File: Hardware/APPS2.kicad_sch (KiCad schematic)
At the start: 18 parts, among them U18 MCP6N11-005, U21 MCP6001

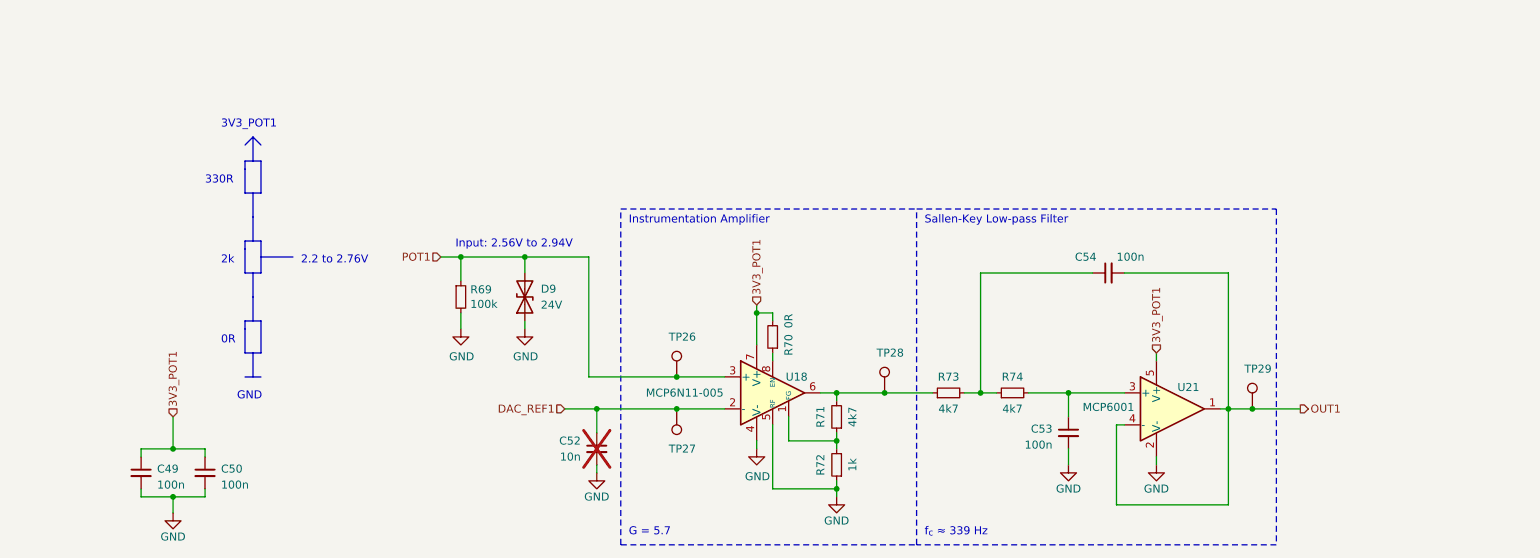
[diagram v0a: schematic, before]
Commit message: Created new hardware version 2.0
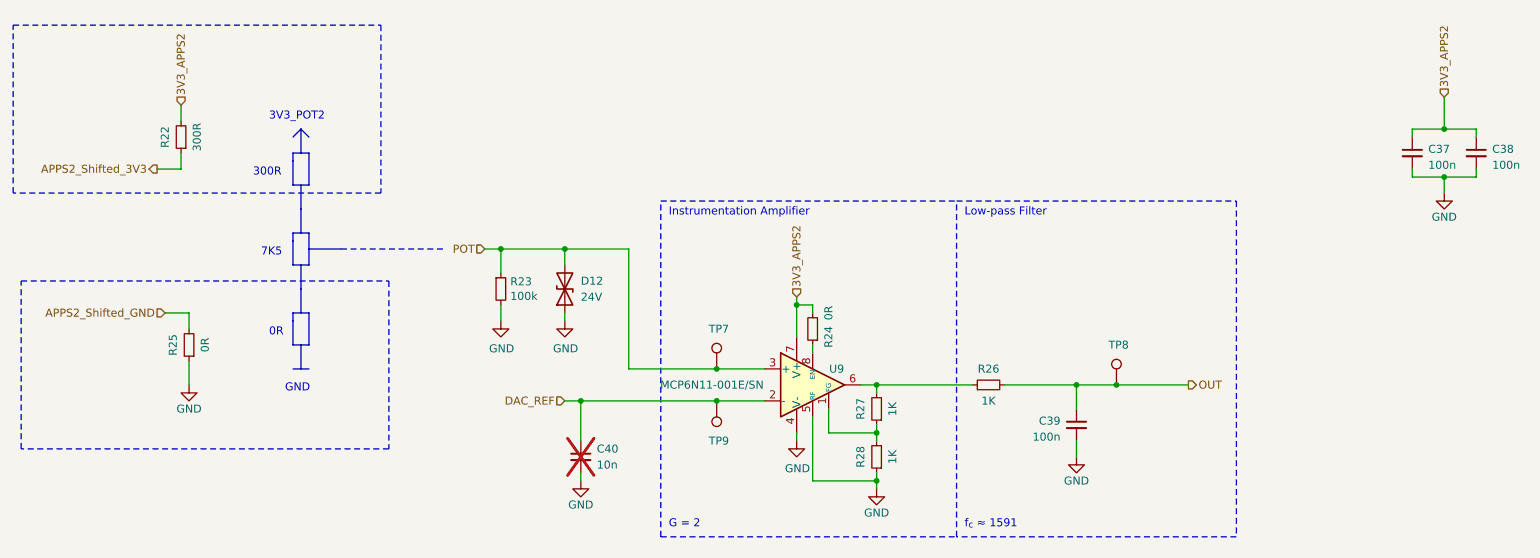
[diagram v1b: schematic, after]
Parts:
- removed C49, C50, C53, C54: 100n, Capacitor_SMD:C_0603_1608Metric_Pad1.08x0.95mm_HandSolder, symbol Device:C_Small
- removed C52: 10n, Capacitor_SMD:C_0603_1608Metric_Pad1.08x0.95mm_HandSolder, symbol Device:C_Small
- removed D9: 24V, Diode_SMD:D_0603_1608Metric_Pad1.05x0.95mm_HandSolder, symbol Device:D_TVS
- removed R69: 100k, Resistor_SMD:R_0603_1608Metric_Pad0.98x0.95mm_HandSolder, symbol Device:R_Small
- removed R70: 0R, Resistor_SMD:R_0603_1608Metric_Pad0.98x0.95mm_HandSolder, symbol Device:R_Small
- removed R71, R73, R74: 4k7, Resistor_SMD:R_0603_1608Metric_Pad0.98x0.95mm_HandSolder, symbol Device:R_Small
- removed R72: 1k, Resistor_SMD:R_0603_1608Metric_Pad0.98x0.95mm_HandSolder, symbol Device:R_Small
- removed TP26: APPS_P, TestPoint:TestPoint_Pad_D1.0mm, symbol Connector:TestPoint
- removed TP27: APPS_N, TestPoint:TestPoint_Pad_D1.0mm, symbol Connector:TestPoint
- removed TP28: APPS_MID, TestPoint:TestPoint_Pad_D1.0mm, symbol Connector:TestPoint
- removed TP29: APPS_OUT, TestPoint:TestPoint_Pad_D1.0mm, symbol Connector:TestPoint
- removed U18: MCP6N11-005, Package_DFN_QFN:TDFN-8-1EP_3x2mm_P0.5mm_EP1.3x1.4mm, symbol MCP6N11:MCP6N11
- removed U21: MCP6001, Package_TO_SOT_SMD:SOT-23-5, symbol Amplifier_Operational:MCP6001-OT
- added C37, C38, C39: 100n, Capacitor_SMD:C_0603_1608Metric_Pad1.08x0.95mm_HandSolder, symbol Device:C_Small
- added C40: 10n, Capacitor_SMD:C_0603_1608Metric_Pad1.08x0.95mm_HandSolder, symbol Device:C_Small
- added D12: 24V, Diode_SMD:D_0603_1608Metric_Pad1.05x0.95mm_HandSolder, symbol Device:D_TVS
- added R22: 300R, Resistor_SMD:R_0603_1608Metric_Pad0.98x0.95mm_HandSolder, symbol Device:R_Small
- added R23: 100k, Resistor_SMD:R_0603_1608Metric_Pad0.98x0.95mm_HandSolder, symbol Device:R_Small
- added R24, R25: 0R, Resistor_SMD:R_0603_1608Metric_Pad0.98x0.95mm_HandSolder, symbol Device:R_Small
- added R26, R27, R28: 1K, Resistor_SMD:R_0603_1608Metric_Pad0.98x0.95mm_HandSolder, symbol Device:R_Small
- added TP7: APPS_P, TestPoint:TestPoint_THTPad_D1.0mm_Drill0.5mm, symbol Connector:TestPoint
- added TP8: APPS_OUT, TestPoint:TestPoint_THTPad_D1.0mm_Drill0.5mm, symbol Connector:TestPoint
- added TP9: APPS_N, TestPoint:TestPoint_THTPad_D1.0mm_Drill0.5mm, symbol Connector:TestPoint
- added U9: MCP6N11-001E/SN, Package_SO:SOIC-8_3.9x4.9mm_P1.27mm, symbol MCP6N11:MCP6N11
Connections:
- net GND: now also C37.2, C38.2, C39.2, C40.2, D12.1 (A1), R23.2, R25.1, R28.1, U9.4 (V-), U9.5 (RF)
- new net: R26.1, R27.2, U9.6
- new net: R27.1, R28.2, U9.1 (FG)
- new net: R24.1, U9.8 (EN)
- new net 3V3_APPS2: C37.1, C38.1, R22.2, R24.2, U9.7 (V+)
- new net APPS2_Shifted_3V3: R22.1
- new net APPS2_Shifted_GND: R25.2
- new net DAC_REF: C40.1, TP9.1, U9.2 (-)
- new net OUT: C39.1, R26.2, TP8.1
- new net POT: D12.2 (A2), R23.1, TP7.1, U9.3 (+)
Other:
- note added: "300R"
- note added: "3V3_POT2"
- note added: "7K5"
- note added: "G = 2"
- note added: "Low-pass Filter"
- note added: "f_{c} ≈ 1591"
- note removed: "2.2 to 2.76V"
- note removed: "2k"
- note removed: "330R"
- note removed: "3V3_POT1"
- note removed: "G = 5.7"
- note removed: "Input: 2.56V to 2.94V"
- note removed: "Sallen-Key Low-pass Filter"
- note removed: "f_{c} ≈ 339 Hz"

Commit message: Changes in schematic, separated CAN buses, added XIAO Sense S3 DevBoard
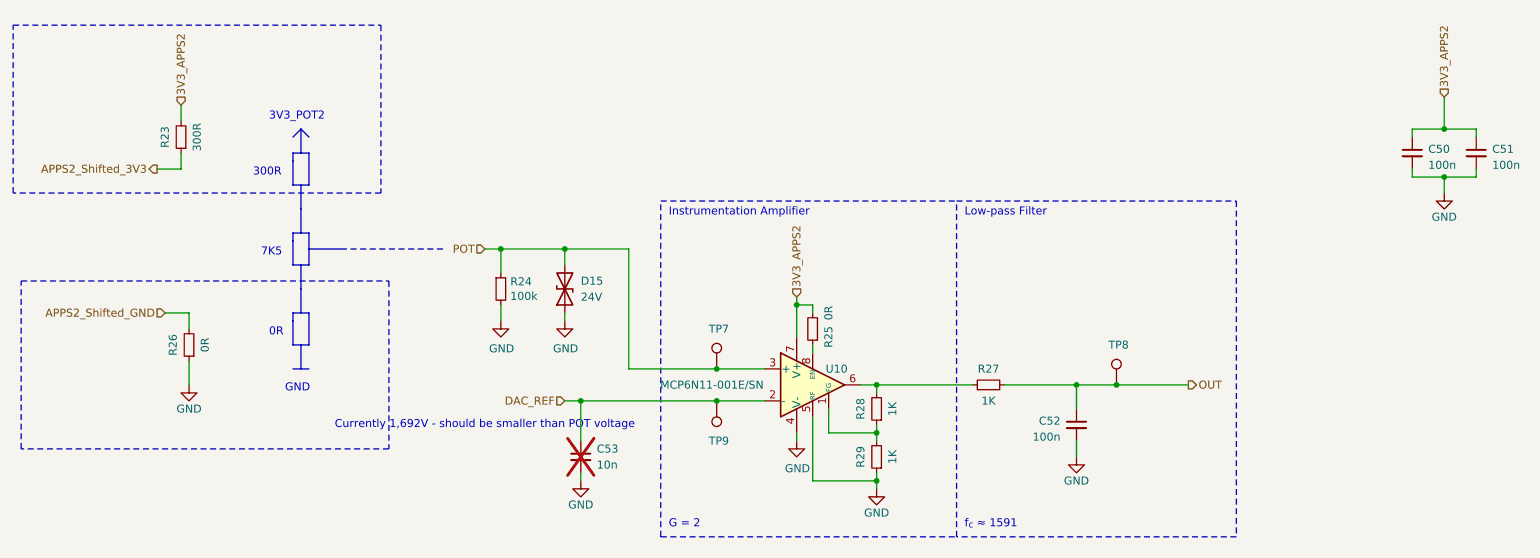
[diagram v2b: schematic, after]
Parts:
- renumbered C37 to C50, C38 to C51, C39 to C52, C40 to C53, D12 to D15, R22 to R23, R23 to R24, R24 to R25, R25 to R26, R26 to R27, R27 to R28, R28 to R29, U9 to U10
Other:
- note added: "Currently 1,692V - should be smaller than POT voltage"

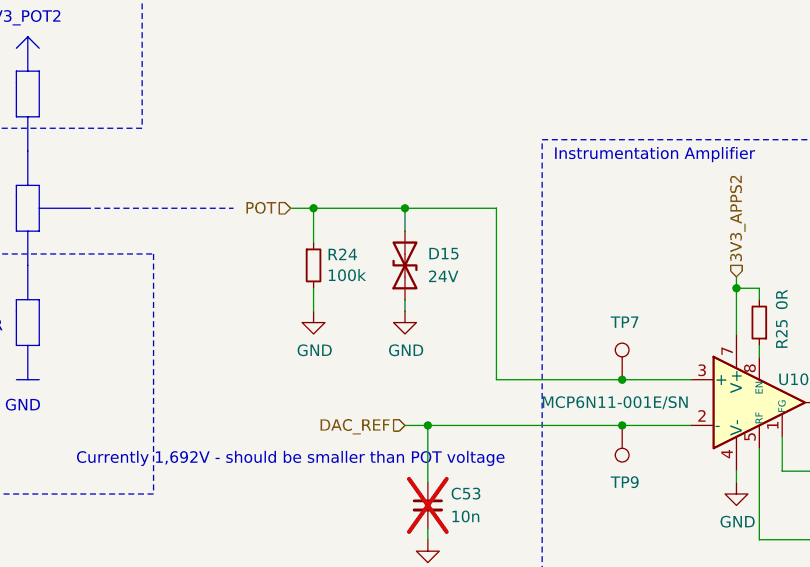
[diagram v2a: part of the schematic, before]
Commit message: Initial layout, changes in safety sensing bus labels
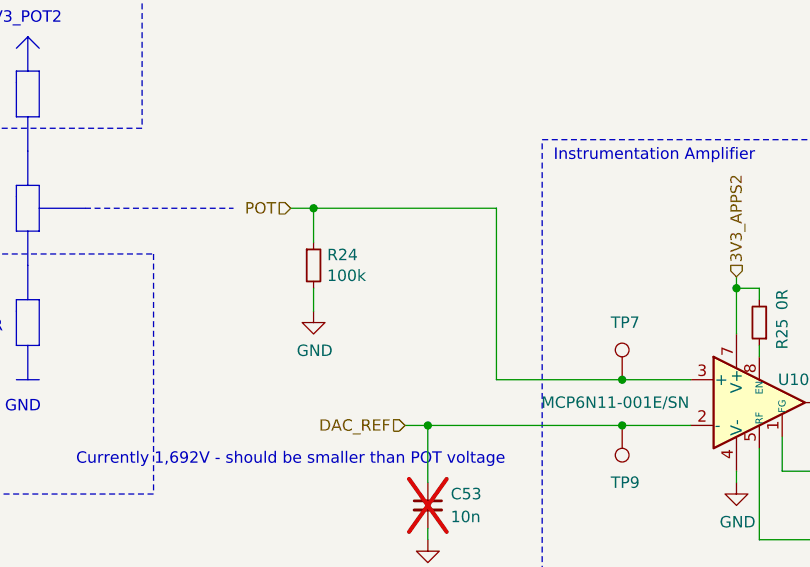
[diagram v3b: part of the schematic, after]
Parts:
- removed D15: 24V, Diode_SMD:D_0603_1608Metric_Pad1.05x0.95mm_HandSolder, symbol Device:D_TVS
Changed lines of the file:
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@@
-	)
-	(junction
-		(at 116.84 73.66)
-		(diameter 0)
-		(color 0 0 0 0)
 	)
 	(junction
@@
 	(wire
 		(pts
-			(xy 116.84 73.66) (xy 127 73.66)
-		)
-		(stroke
-			(width 0)
-			(type default)
-		)
-	)
-	(wire
-		(pts
 			(xy 166.37 95.25) (xy 166.37 96.52)
 		)
@@
 	(wire
 		(pts
-			(xy 106.68 73.66) (xy 116.84 73.66)
+			(xy 106.68 73.66) (xy 127 73.66)
 		)
 		(stroke
@@
 	(wire
 		(pts
-			(xy 116.84 76.2) (xy 116.84 73.66)
-		)
-		(stroke
-			(width 0)
-			(type default)
-		)
-	)
-	(wire
-		(pts
 			(xy 158.75 102.87) (xy 166.37 102.87)
 		)
@@
 		(pts
 			(xy 106.68 77.47) (xy 106.68 73.66)
-		)
-		(stroke
-			(width 0)
-			(type default)
-		)
-	)
-	(wire
-		(pts
-			(xy 116.84 85.09) (xy 116.84 83.82)
 		)
 		(stroke
@@
 	)
 	(symbol
-		(lib_id "Device:D_TVS")
-		(at 116.84 80.01 90)
-		(unit 1)
-		(exclude_from_sim no)
-		(in_bom yes)
-		(on_board yes)
-		(dnp no)
-		(fields_autoplaced yes)
-		(property "Reference" "D15"
-			(at 119.38 78.74 90)
-			(effects
-				(font
-					(size 1.27 1.27)
-				)
-				(justify right)
-			)
-		)
-		(property "Value" "24V"
-			(at 119.38 81.28 90)
-			(effects
-				(font
-					(size 1.27 1.27)
-				)
-				(justify right)
-			)
-		)
-		(property "Footprint" "Diode_SMD:D_0603_1608Metric_Pad1.05x0.95mm_HandSolder"
-			(at 116.84 80.01 0)
-			(effects
-				(font
-					(size 1.27 1.27)
-				)
-				(hide yes)
-			)
-		)
-		(property "Datasheet" "~"
-			(at 116.84 80.01 0)
-			(effects
-				(font
-					(size 1.27 1.27)
-				)
-				(hide yes)
-			)
-		)
-		(property "Description" ""
-			(at 116.84 80.01 0)
-			(effects
-				(font
-					(size 1.27 1.27)
-				)
-				(hide yes)
-			)
-		)
-		(pin "1"
-		)
-		(pin "2"
-		)
-		(instances
-			(project "PUTM_EV_Frontbox"
-				(path "/b652b05a-4e3d-4ad1-b032-18886abe7d45/b86dc381-cd35-4cf0-a864-717359311087"
-					(reference "D15")
-					(unit 1)
-				)
-			)
-		)
-	)
-	(symbol
 		(lib_id "Connector:TestPoint")
 		(at 204.47 95.25 0)
@@
 					(unit 1)
 				)
-			)
-		)
-	)
-	(symbol
-		(lib_id "power:GND")
-		(at 116.84 85.09 0)
-		(unit 1)
-		(exclude_from_sim no)
-		(in_bom yes)
-		(on_board yes)
-		(dnp no)
-		(property "Reference" "#PWR082"
-			(at 116.84 91.44 0)
-			(effects
-				(font
-					(size 1.27 1.27)
-				)
-				(hide yes)
-			)
-		)
-		(property "Value" "GND"
-			(at 116.967 89.4842 0)
-			(effects
-				(font
-					(size 1.27 1.27)
-				)
-			)
-		)
-		(property "Footprint" ""
-			(at 116.84 85.09 0)
-			(effects
-				(font
-					(size 1.27 1.27)
-				)
-				(hide yes)
-			)
-		)
-		(property "Datasheet" ""
-			(at 116.84 85.09 0)
-			(effects
-				(font
-					(size 1.27 1.27)
-				)
-				(hide yes)
-			)
-		)
-		(property "Description" ""
-			(at 116.84 85.09 0)
-			(effects
-				(font
-					(size 1.27 1.27)
-				)
-				(hide yes)
-			)
-		)
-		(pin "1"
-		)
-		(instances
-			(project "PUTM_EV_Frontbox"
-				(path "/b652b05a-4e3d-4ad1-b032-18886abe7d45/b86dc381-cd35-4cf0-a864-717359311087"
-					(reference "#PWR082")
-					(unit 1)
-				)

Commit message: Changes in CAN section
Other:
- title: (none) -> FrontBox
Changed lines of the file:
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@@
 	(generator_version "9.0")
 	(paper "A4")
+	(title_block
+		(title "FrontBox")
+	)
 	(rectangle
 		(start 30.48 78.74)

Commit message: BOM update
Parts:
- C50, C51, C52, C53, R23, R24, R25, R26, R27, R28, R29: Mouser Part Number (none) -> .
- U10: Mouser Part Number (none) -> 579-MCP6N11-001E/SN
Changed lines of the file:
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@@
+			)
+		)
+		(property "Mouser Part Number" "."
+			(at 184.15 95.25 0)
+			(effects
+				(font
+					(size 1.27 1.27)
+				)
 			)
 		)
@@
 			)
 		)
+		(property "Mouser Part Number" "."
+			(at 198.12 101.6 0)
+			(effects
+				(font
+					(size 1.27 1.27)
+				)
+			)
+		)
 		(pin "1"
 		)
@@
 			)
 		)
+		(property "Mouser Part Number" "."
+			(at 251.46 58.42 0)
+			(effects
+				(font
+					(size 1.27 1.27)
+				)
+			)
+		)
 		(pin "1"
 		)
@@
 			)
 		)
+		(property "Mouser Part Number" "."
+			(at 261.62 58.42 0)
+			(effects
+				(font
+					(size 1.27 1.27)
+				)
+			)
+		)
 		(pin "1"
 		)
@@
 			)
 		)
+		(property "Mouser Part Number" "."
+			(at 166.37 99.06 0)
+			(effects
+				(font
+					(size 1.27 1.27)
+				)
+			)
+		)
 		(pin "1"
 		)
@@
 			)
 		)
+		(property "Mouser Part Number" "."
+			(at 55.88 55.88 0)
+			(effects
+				(font
+					(size 1.27 1.27)
+				)
+			)
+		)
 		(pin "1"
 		)
@@
 				)
 				(hide yes)
+			)
+		)
+		(property "Mouser Part Number" "."
+			(at 166.37 106.68 0)
+			(effects
+				(font
+					(size 1.27 1.27)
+				)
 			)
 		)
@@
 			)
 		)
+		(property "Mouser Part Number" "."
+			(at 119.38 106.68 0)
+			(effects
+				(font
+					(size 1.27 1.27)
+				)
+			)
+		)
 		(pin "1"
 		)
@@
 			)
 		)
+		(property "Mouser Part Number" "."
+			(at 57.15 88.9 0)
+			(effects
+				(font
+					(size 1.27 1.27)
+				)
+			)
+		)
 		(pin "1"
 		)
@@
 			)
 		)
+		(property "Mouser Part Number" "."
+			(at 156.21 86.36 0)
+			(effects
+				(font
+					(size 1.27 1.27)
+				)
+			)
+		)
 		(pin "1"
 		)
@@
 			)
 		)
+		(property "Mouser Part Number" "579-MCP6N11-001E/SN"
+			(at 156.21 95.25 0)
+			(effects
+				(font
+					(size 1.27 1.27)
+				)
+				(hide yes)
+			)
+		)
 		(pin "1"
 		)
@@
 			)
 		)
+		(property "Mouser Part Number" "."
+			(at 106.68 80.01 0)
+			(effects
+				(font
+					(size 1.27 1.27)
+				)
+			)
+		)

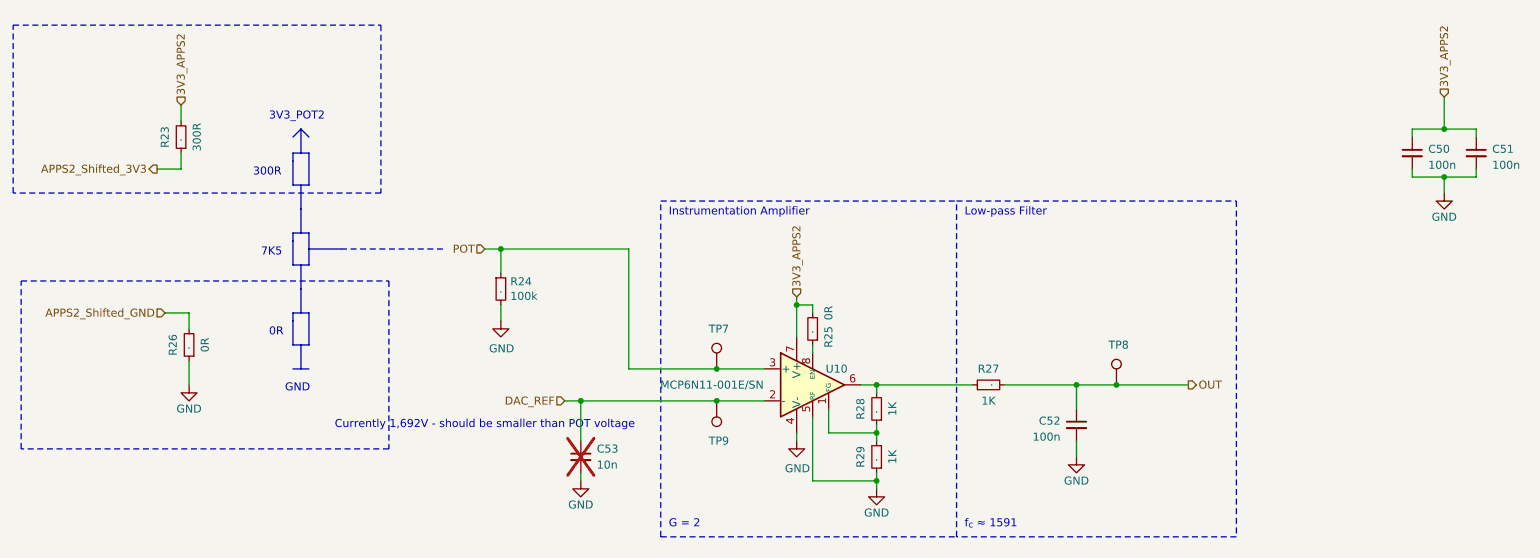
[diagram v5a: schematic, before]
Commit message: Added tensionmeter section, updated APPS resistors for transfer function
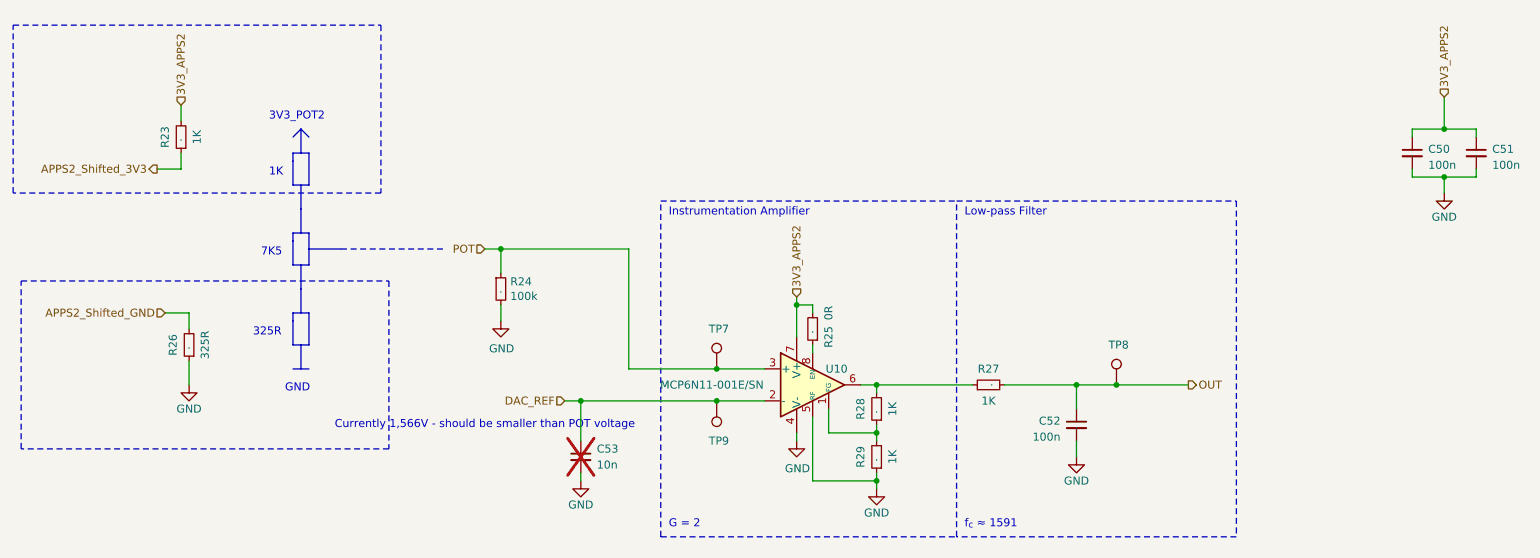
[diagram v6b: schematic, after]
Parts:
- R23: value 300R -> 1K
- R26: value 0R -> 325R
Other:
- note added: "1K"
- note added: "325R"
- note added: "Currently 1,566V - should be smaller than POT voltage"
- note removed: "0R"
- note removed: "300R"
- note removed: "Currently 1,692V - should be smaller than POT voltage"
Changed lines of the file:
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@@
 		)
 	)
-	(text "300R\n"
-		(exclude_from_sim no)
-		(at 67.31 62.23 0)
+	(text "1K\n"
+		(exclude_from_sim no)
+		(at 69.85 62.23 0)
 		(effects
 			(font
@@
 		)
 	)
-	(text "Currently 1,692V - should be smaller than POT voltage\n"
+	(text "Currently 1,566V - should be smaller than POT voltage\n"
 		(exclude_from_sim no)
 		(at 104.14 101.6 0)
@@
 		)
 	)
-	(text "0R\n"
-		(exclude_from_sim no)
-		(at 69.85 87.63 0)
+	(text "325R\n"
+		(exclude_from_sim no)
+		(at 67.31 87.63 0)
 		(effects
 			(font
@@
 			)
 		)
-		(property "Value" "300R"
+		(property "Value" "1K"
 			(at 58.42 55.88 90)
 			(effects
@@
 			)
 		)
-		(property "Value" "0R"
+		(property "Value" "325R"
 			(at 59.69 88.9 90)
 			(effects
